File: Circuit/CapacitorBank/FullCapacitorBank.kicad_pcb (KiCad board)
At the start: 2 copper layers, 189.2 x 61 mm, 50 parts, among them J1 AC Power In, J2 Output+, J3 Output-, J4 To Voltage Sensing, Q1 BT138-800, Q2 BT138-800, SW1 SW_Push, T1 6:75+75, U1 PC817, U2 PC817

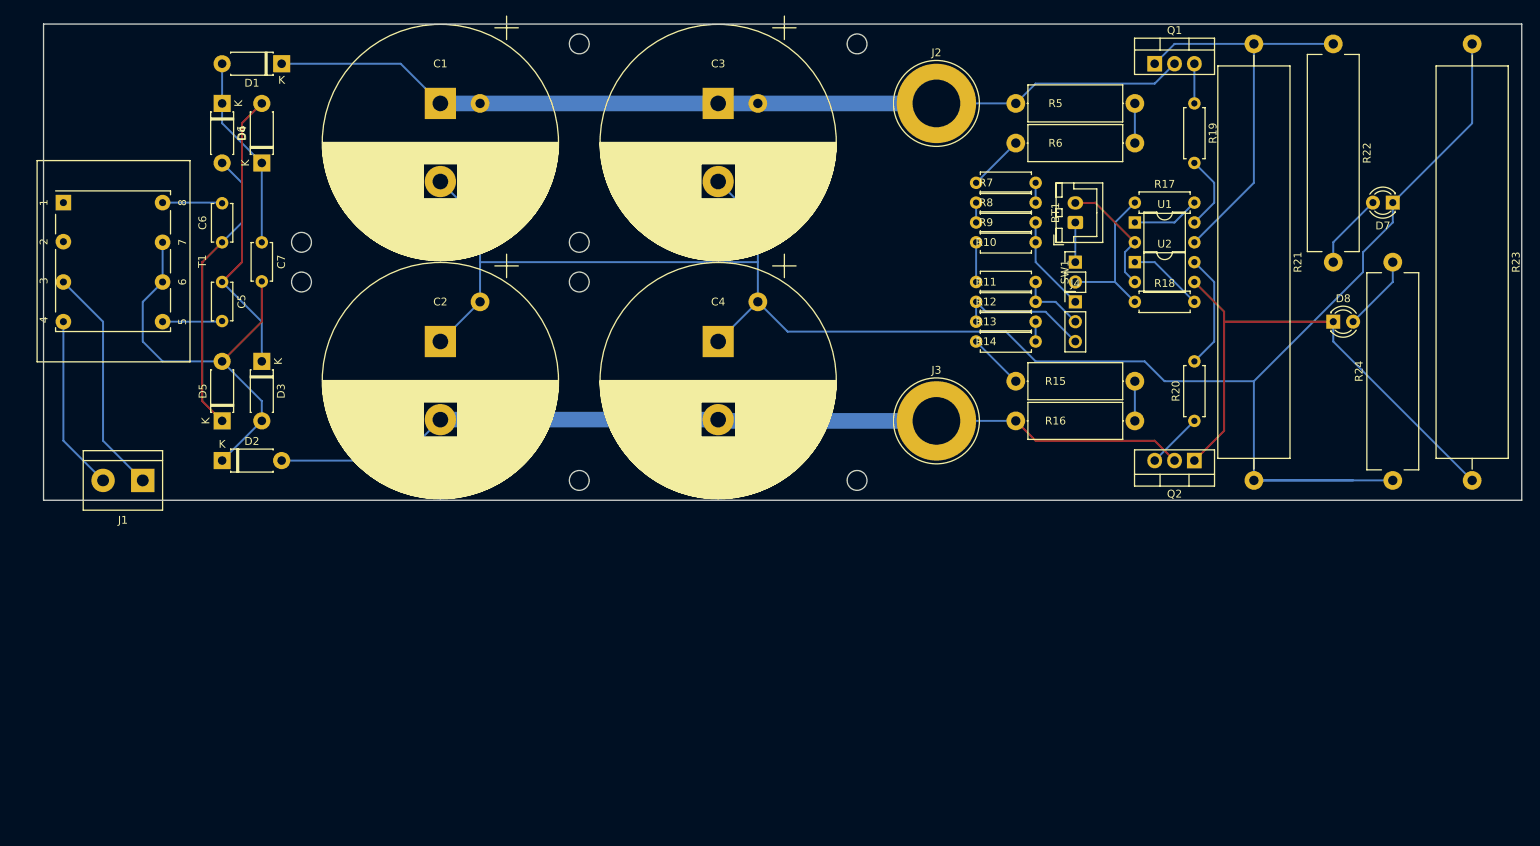
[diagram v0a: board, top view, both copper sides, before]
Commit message: [Circuit] Optimize the layout of PCBs
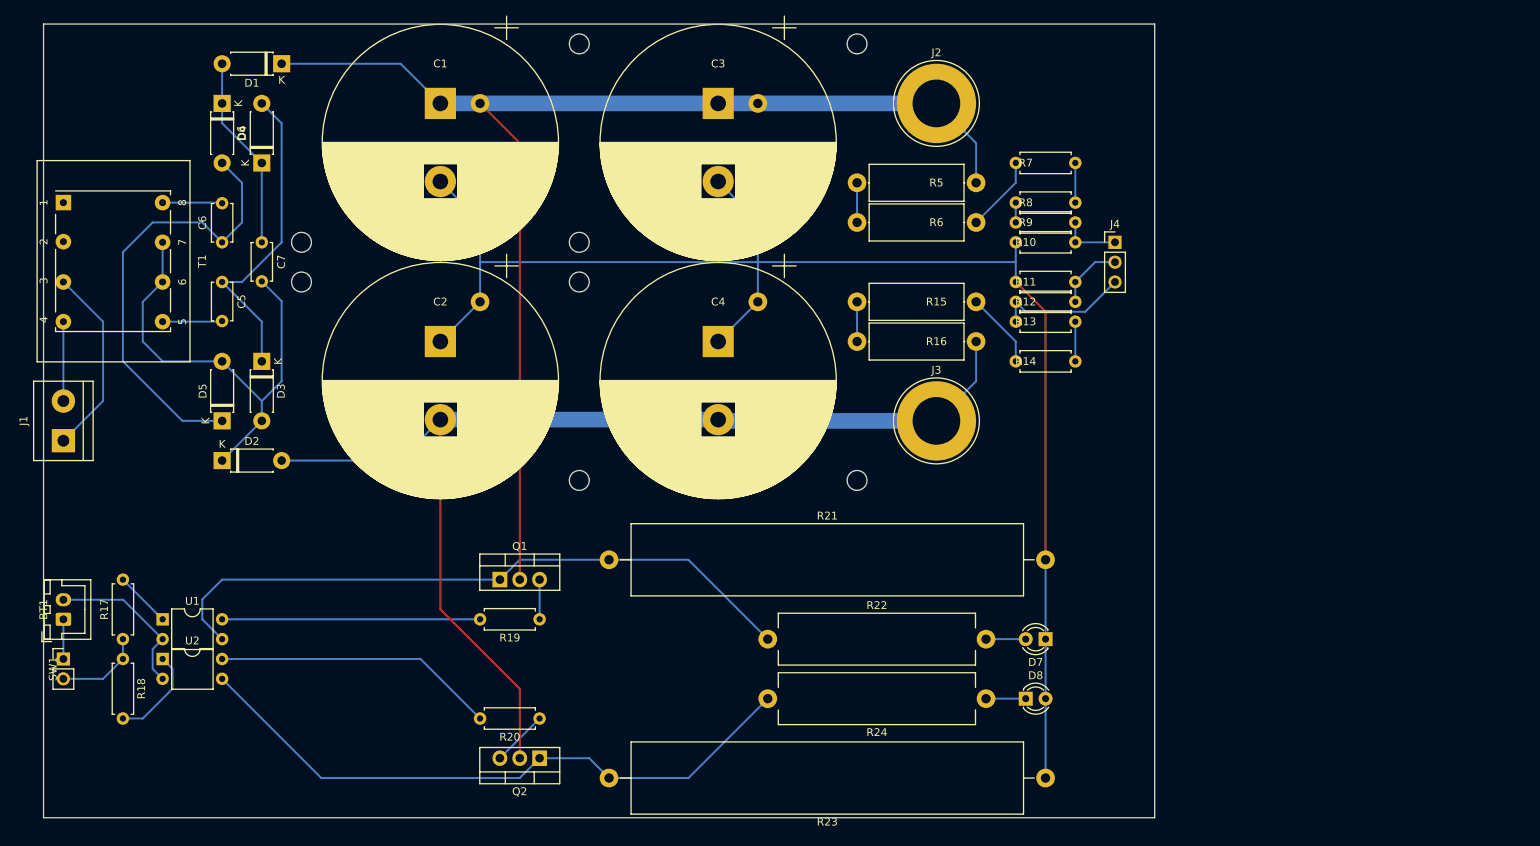
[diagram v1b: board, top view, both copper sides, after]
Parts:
- moved R17 141.1 mm to (55.9, 111.8), turned to 90 degrees
- moved BT1 139.1 mm to (48.3, 109.2)
- moved SW1 139.1 mm to (48.3, 114.3)
- moved R18 137.4 mm to (55.9, 114.3), turned to 270 degrees
- moved U1 134.4 mm to (61.0, 109.2)
- moved U2 134.4 mm to (61.0, 114.3)
- moved R23 108.7 mm to (174.0, 129.5), turned to 180 degrees
- moved Q1 106.7 mm to (104.1, 104.1)
- moved R19 106.7 mm to (109.2, 109.2), turned to 180 degrees
- moved R21 105.7 mm to (118.1, 101.6), turned to 0 degrees
- moved R22 105.1 mm to (138.4, 111.8), turned to 0 degrees
- moved R20 92.1 mm to (109.2, 121.9), turned to 180 degrees
- moved Q2 92.1 mm to (109.2, 127.0)
- moved D7 71.4 mm to (174.0, 111.8)
- moved D8 62.3 mm to (171.4, 119.4)
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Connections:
- D8 pad 2: Net-(D8-Pad2) -> Net-(C1-Pad2)
- Q2 pad 1: Net-(D8-Pad1) -> Net-(Q2-Pad1)
- R10 pad 2: Net-(R10-Pad2) -> Net-(C1-Pad2)
- R11 pad 1: Net-(R10-Pad2) -> Net-(C1-Pad2)
- R23 pad 2: Net-(D8-Pad1) -> Net-(Q2-Pad1)
- R24 pad 1: Net-(C1-Pad2) -> Net-(D8-Pad1)
- R24 pad 2: Net-(D8-Pad2) -> Net-(Q2-Pad1)
- U2 pad 3: Net-(D8-Pad1) -> Net-(Q2-Pad1)
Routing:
- net Net-(Q2-Pad1): track 0.00 -> 81.4 mm
- net Net-(D8-Pad1): track 67.7 -> 5.08 mm
- net Net-(C1-Pad2): track 250.7 -> 188.2 mm
- net /PowerOut+: track 118.5 -> 161.3 mm
- net Net-(Q1-Pad1): track 52.5 -> 84.8 mm
- net /PowerOut-: track 118.4 -> 145.6 mm
- net Net-(R19-Pad2): track 9.72 -> 33.0 mm
- net Net-(R20-Pad2): track 14.8 -> 36.2 mm
- net Net-(C6-Pad1): track 37.2 -> 57.4 mm
- net /ACPowerIn-: track 22.4 -> 10.2 mm
- net Net-(D8-Pad2): track 9.72 -> 0.00 mm
- net Net-(R17-Pad1): track 19.9 -> 11.2 mm
- net Net-(R10-Pad2): track 5.08 -> 0.00 mm
- net Net-(C7-Pad2): track 54.2 -> 59.3 mm
- net /ACPowerIn+: track 29.6 -> 24.5 mm
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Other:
- board size 189.2 x 61 mm -> 142.2 x 101.6 mm

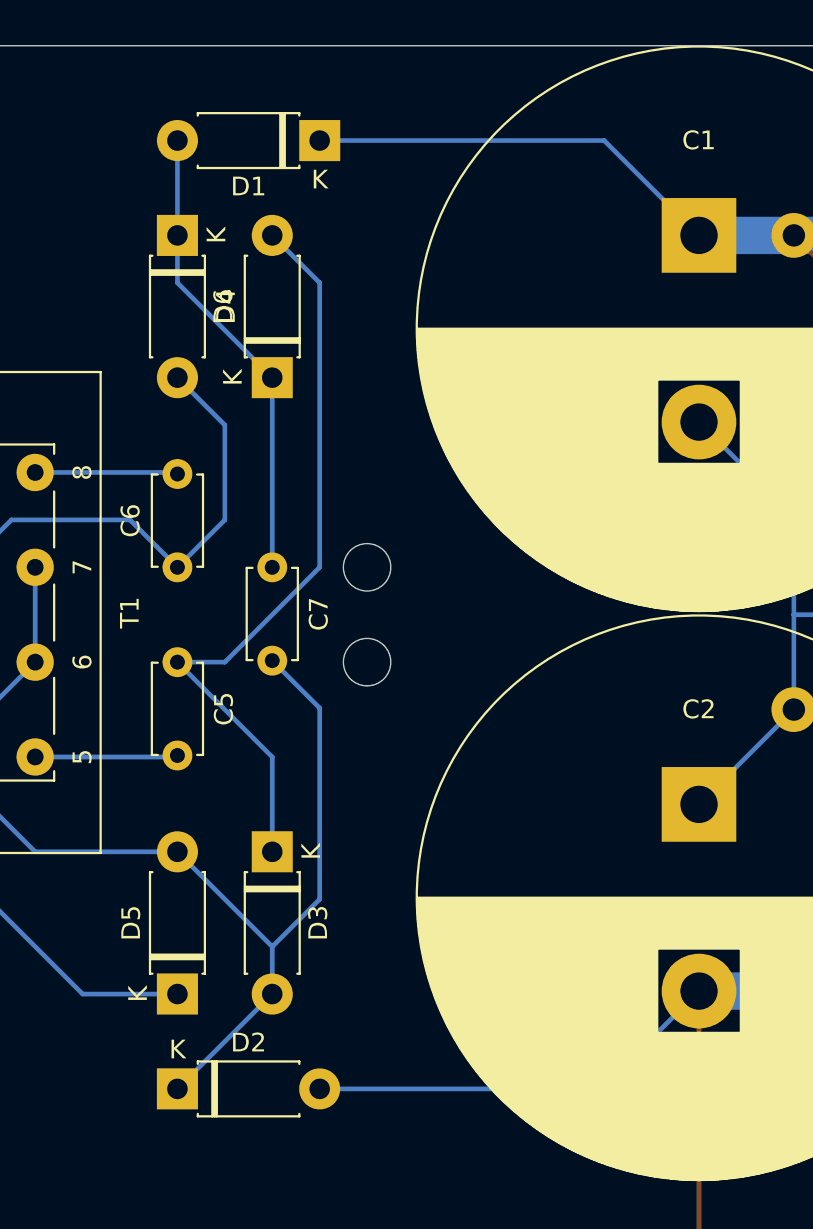
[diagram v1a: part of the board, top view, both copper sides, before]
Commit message: [Circuit] Fine tune some pcb layouts
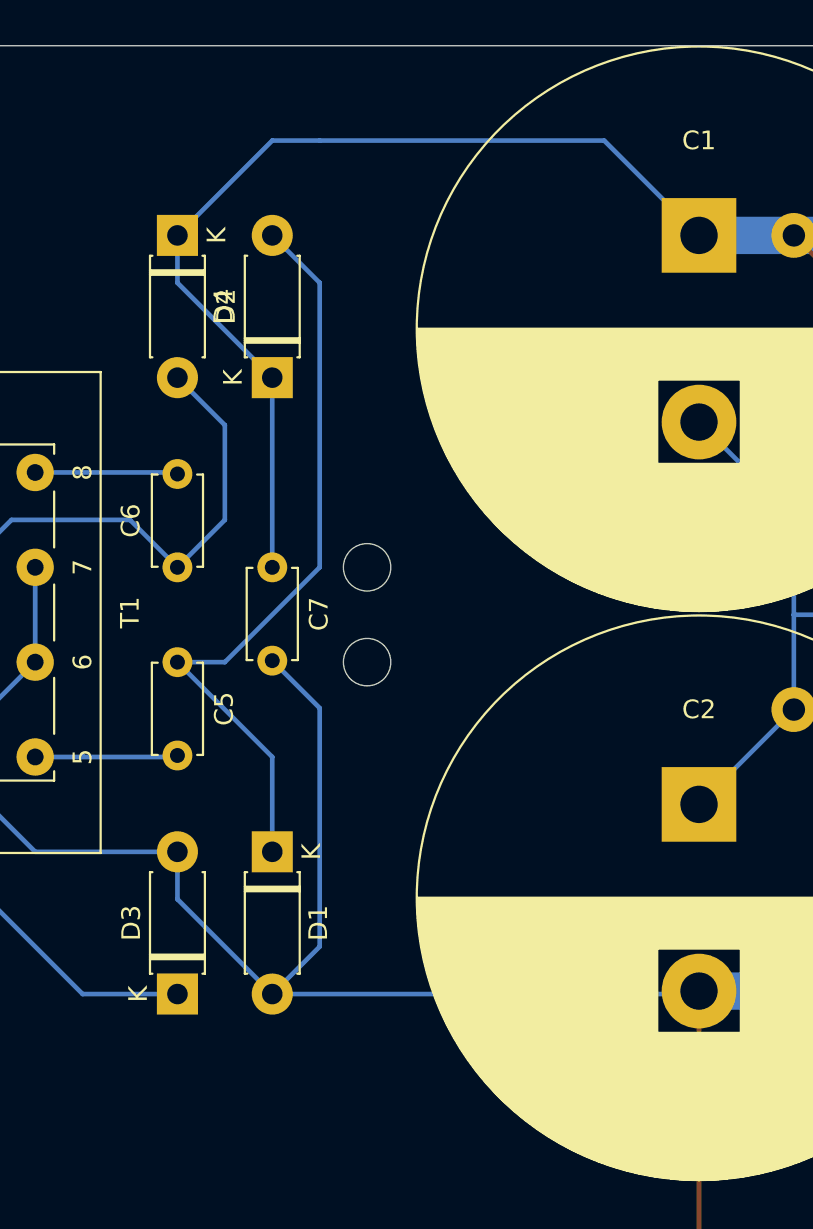
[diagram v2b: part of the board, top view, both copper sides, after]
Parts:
- removed the D1 at (76.2, 38.1)
- removed the D2 at (68.6, 88.9)
- renumbered D3 to D1, D4 to D2, D5 to D3, D6 to D4
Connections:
- C7 pad 1: Net-(C7-Pad1) -> /PowerOut+
- C7 pad 2: Net-(C7-Pad2) -> /PowerOut-
- D1 pad 2: Net-(C7-Pad2) -> /PowerOut-
- D2 pad 1: Net-(C7-Pad1) -> /PowerOut+
- D3 pad 2: Net-(C7-Pad2) -> /PowerOut-
- D4 pad 1: Net-(C7-Pad1) -> /PowerOut+
- T1 pad 6: Net-(C7-Pad2) -> /PowerOut-
- T1 pad 7: Net-(C7-Pad2) -> /PowerOut-
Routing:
- net Net-(C7-Pad2): track 59.3 -> 0.00 mm
- net /PowerOut-: track 145.6 -> 200.7 mm
- net /PowerOut+: track 161.3 -> 190.9 mm
- net Net-(C7-Pad1): track 25.0 -> 0.00 mm

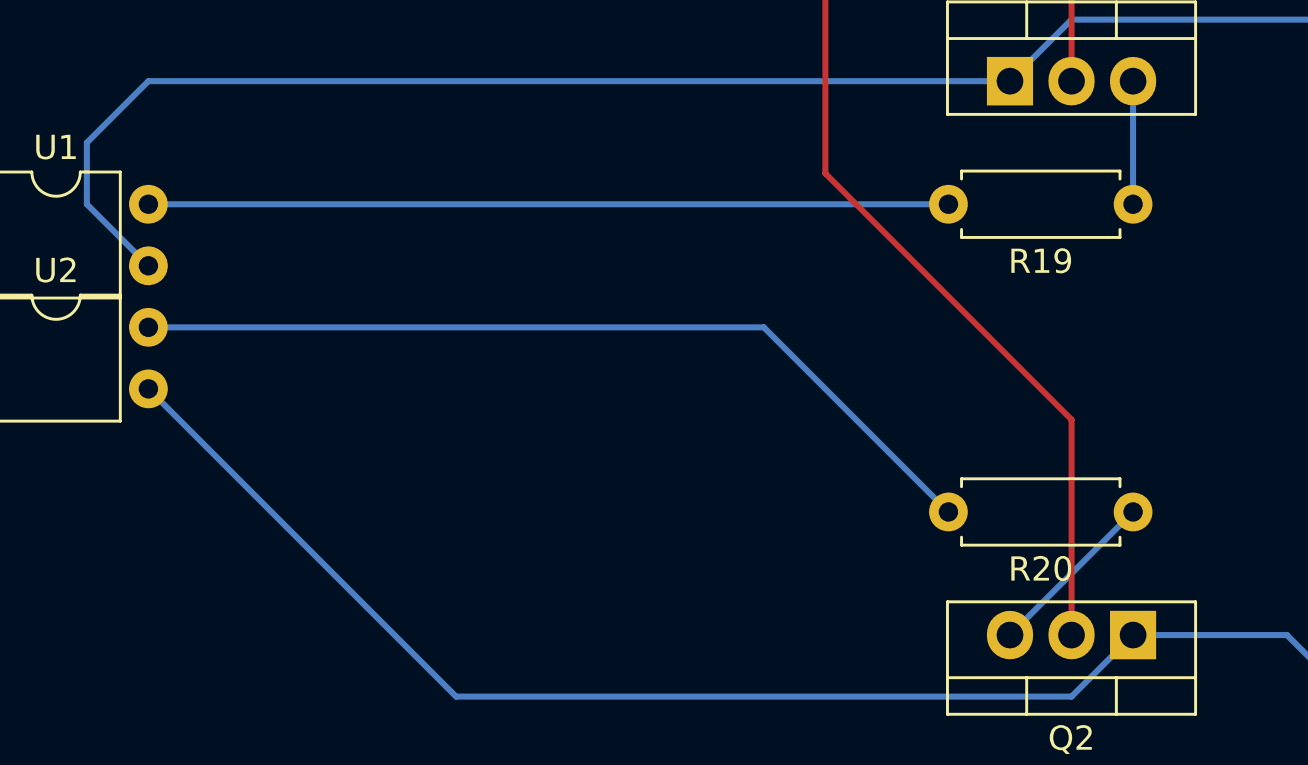
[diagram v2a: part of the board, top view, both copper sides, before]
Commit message: [Circuit] Adjust resistors in capacitor bank
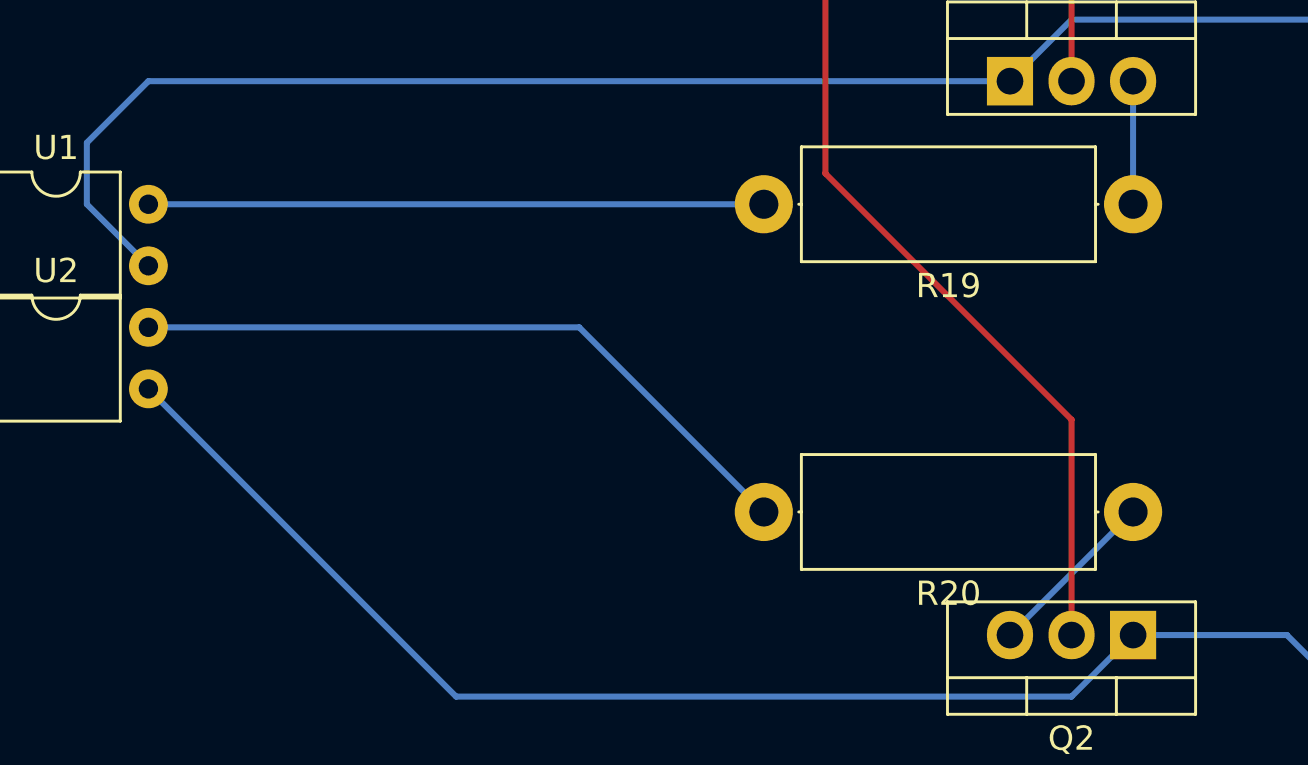
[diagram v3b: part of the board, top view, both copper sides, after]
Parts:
- R1, R2, R3, R4: value 1M -> 1M/1W
- R19, R20: value 10K -> 1M/1W; footprint Resistor_THT:R_Axial_DIN0207_L6.3mm_D2.5mm_P7.62mm_Horizontal -> Resistor_THT:R_Axial_DIN0414_L11.9mm_D4.5mm_P15.24mm_Horizontal
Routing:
- net Net-(R20-Pad2): track 36.2 -> 28.6 mm
- net Net-(R19-Pad2): track 33.0 -> 25.4 mm
